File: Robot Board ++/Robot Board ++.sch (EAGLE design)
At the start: 127 parts, among them U5 TPS5331[8/9].DQP

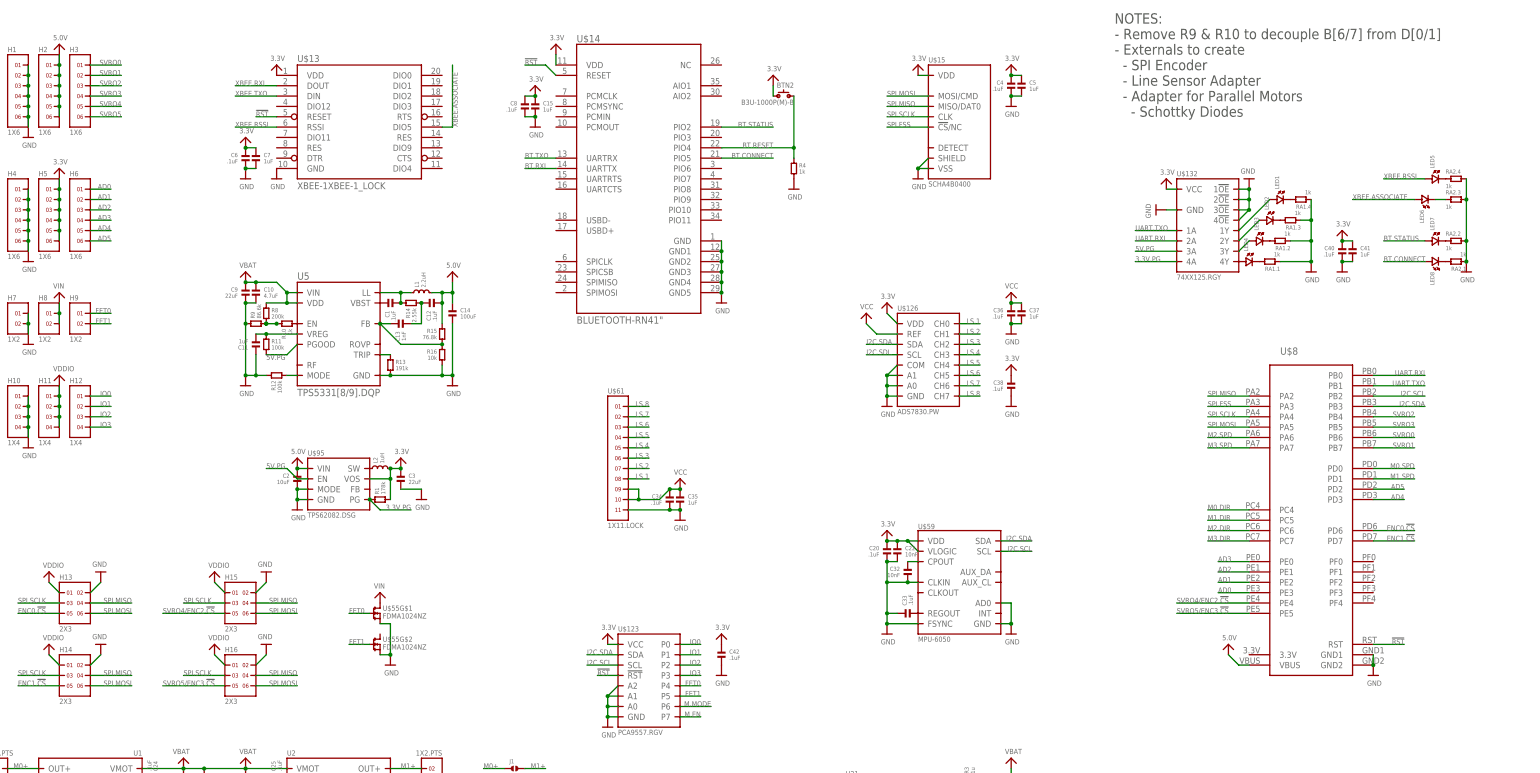
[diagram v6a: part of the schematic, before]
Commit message: Fixed Mosfet connections in Schematic Fixed 3.3v rail in Shcematic (3.3v meant to be decoupled between boards) Began routing signals on PCB
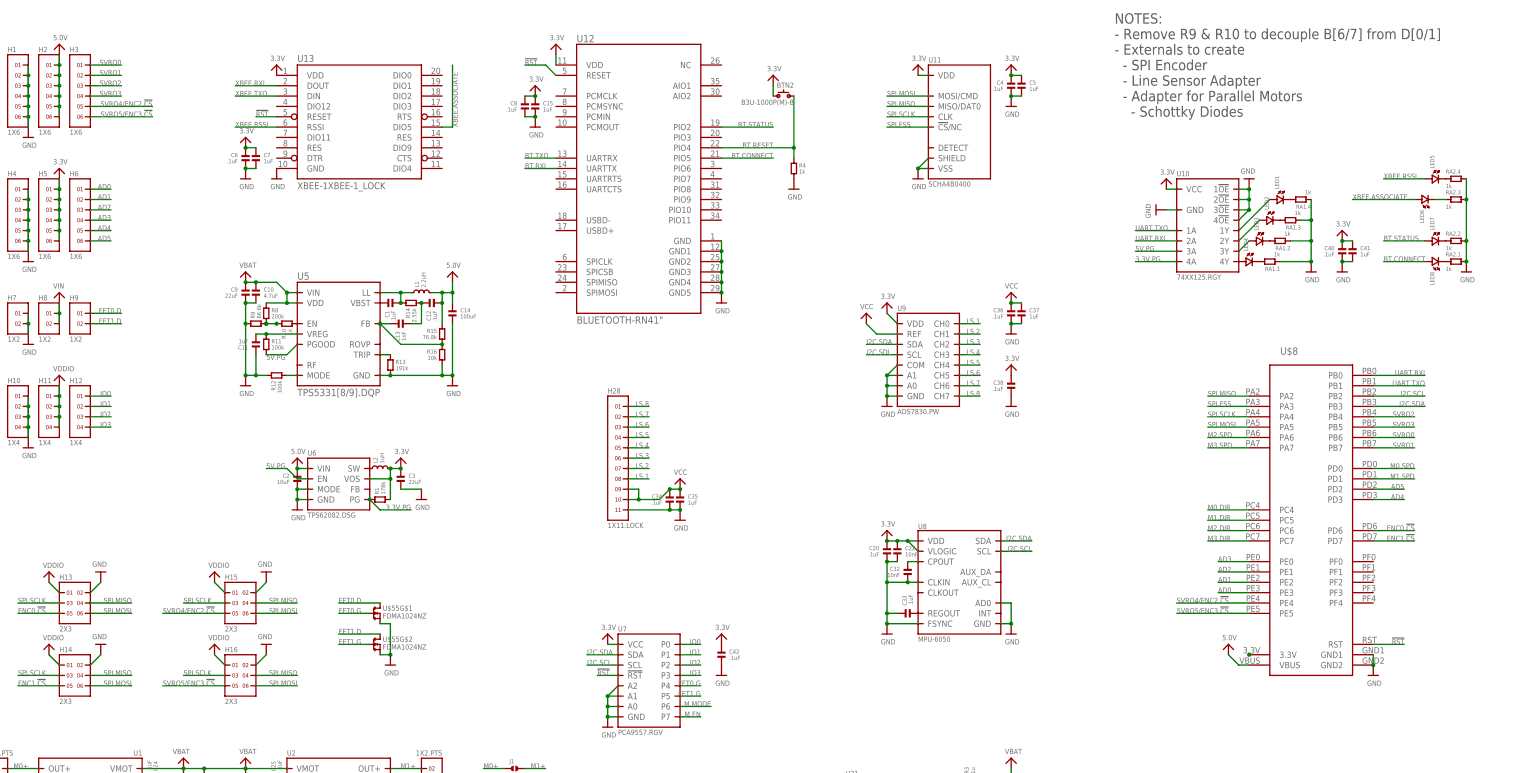
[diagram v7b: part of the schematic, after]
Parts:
- renumbered U$123 to U7, U$126 to U9, U$13 to U13, U$132 to U10, U$14 to U12, U$15 to U11, U$59 to U8, U$61 to H28, U$95 to U6
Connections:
- removed net FET0: H9.1, U$55G$1.G, U7.P4
- removed net FET1: H9.2, U$55G$2.G, U7.P5
- removed net N$45: LED8.2, RA2.1.2
- removed net SVRO4: H3.5
- removed net SVRO5: H3.6
- new net FET0.D: H9.1, U$55G$1.D
- new net FET0.G: U$55G$1.G, U7.P4
- new net FET1.D: H9.2, U$55G$2.D
- new net FET1.G: U$55G$2.G, U7.P5
- new net N$1: U$8.3.3V
- new net N$9: LED8.2, RA2.1.1
- net GND: now also RA2.1.2; no longer RA2.1.1
- net SVRO4/ENC2.!CS: now also H3.5
- net SVRO5/ENC3.!CS: now also H3.6
- net VIN: no longer U$55G$1.D
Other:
- moved on the sheet: RA2.1

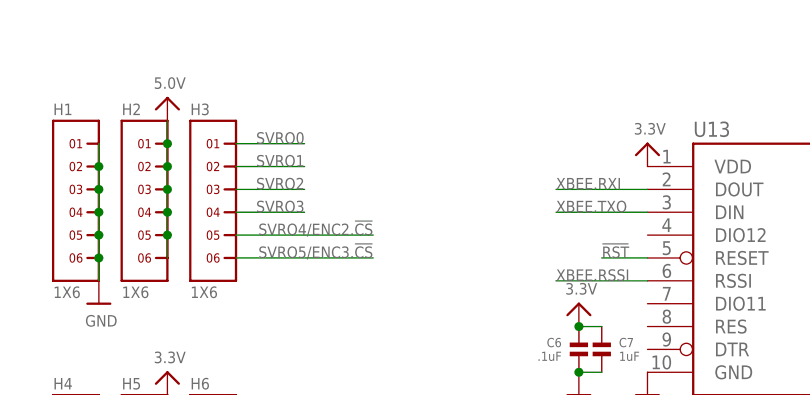
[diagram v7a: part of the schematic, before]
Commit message: Added 100uF capacitor to Servo Lines
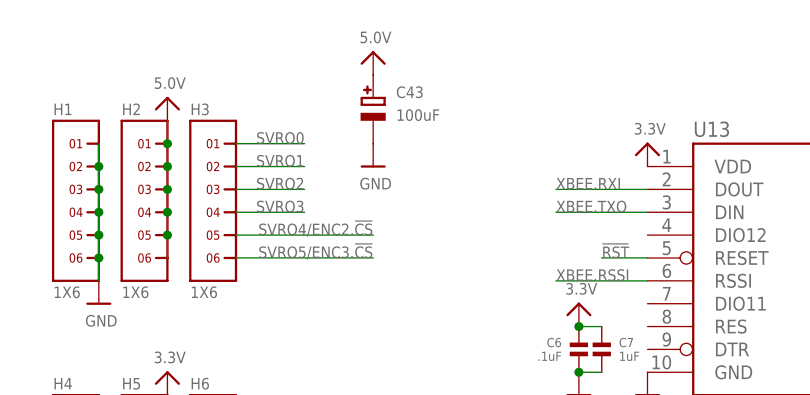
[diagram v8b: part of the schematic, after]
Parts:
- added C43: 100uF, microbuilder:CAP_ELECTROLYTICPANASONIC_C
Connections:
- net 5.0V: now also C43.+
- net GND: now also C43.-
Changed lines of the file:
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@@
 <part name="U$138" library="microbuilder" deviceset="3.3V" device=""/>
 <part name="U$1" library="microbuilder" deviceset="5.0V" device=""/>
+<part name="C43" library="microbuilder" deviceset="CAP_ELECTROLYTIC" device="PANASONIC_C" value="100uF"/>
+<part name="U$2" library="microbuilder" deviceset="5.0V" device=""/>
+<part name="U$5" library="microbuilder" deviceset="GND" device=""/>
 </parts>
 <sheets>
@@
 <instance part="U$138" gate="G$1" x="180.34" y="15.24"/>
 <instance part="U$1" gate="G$1" x="312.42" y="96.52"/>
+<instance part="C43" gate="G$1" x="48.26" y="241.3"/>
+<instance part="U$2" gate="G$1" x="48.26" y="248.92"/>
+<instance part="U$5" gate="G$1" x="48.26" y="236.22"/>
 </instances>
 <busses>
@@
 <junction x="370.84" y="190.5"/>
 </segment>
+<segment>
+<pinref part="C43" gate="G$1" pin="-"/>
+<pinref part="U$5" gate="G$1" pin="GND"/>
+</segment>
 </net>
 <net name="3.3V" class="0">
@@
 <wire x1="314.96" y1="91.44" x2="312.42" y2="93.98" width="0.1524" layer="91"/>
 </segment>
-</net>
+<segment>
+<pinref part="C43" gate="G$1" pin="+"/>
+<pinref part="U$2" gate="G$1" pin="5.0V"/>
+</segment>
+</net>
